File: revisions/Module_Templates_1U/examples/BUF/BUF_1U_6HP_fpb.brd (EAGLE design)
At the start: 28.4 x 28.4 mm, 11 parts, among them J2 ERA-NOSILK

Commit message: Update Backplane Reference
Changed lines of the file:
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@@
 <setting verticaltext="up"/>
 </settings>
-<grid distance="10" unitdist="mil" unit="mil" style="lines" multiple="10" display="yes" altdistance="0.025" altunitdist="inch" altunit="inch"/>
+<grid distance="10" unitdist="mil" unit="mm" style="lines" multiple="10" display="yes" altdistance="0.025" altunitdist="inch" altunit="inch"/>
 <layers>
 <layer number="1" name="Top" color="4" fill="1" visible="no" active="yes"/>
@@
 <layer number="220" name="220bmp" color="21" fill="1" visible="no" active="no"/>
 <layer number="221" name="221bmp" color="22" fill="1" visible="no" active="no"/>
-<layer number="222" name="222bmp" color="23" fill="1" visible="no" active="no"/>
 <layer number="223" name="223bmp" color="24" fill="1" visible="no" active="no"/>
 <layer number="224" name="224bmp" color="25" fill="1" visible="no" active="no"/>
@@
 <circle x="5.08" y="40.1828" radius="1.905" width="0.4064" layer="51"/>
 <circle x="5.08" y="2.9972" radius="1.9235375" width="0.4064" layer="51"/>
-<text x="8.382" y="7.62" size="1.27" layer="21" font="vector" ratio="20">Halcyon Modular</text>
 <text x="23.876" y="8.89" size="1.27" layer="22" font="vector" ratio="20" rot="R180">Halcyon Modular</text>
 </plain>

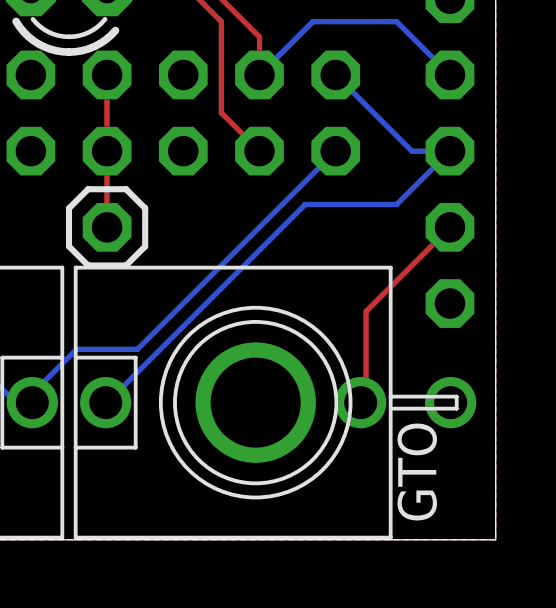
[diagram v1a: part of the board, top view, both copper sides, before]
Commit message: update backplane images
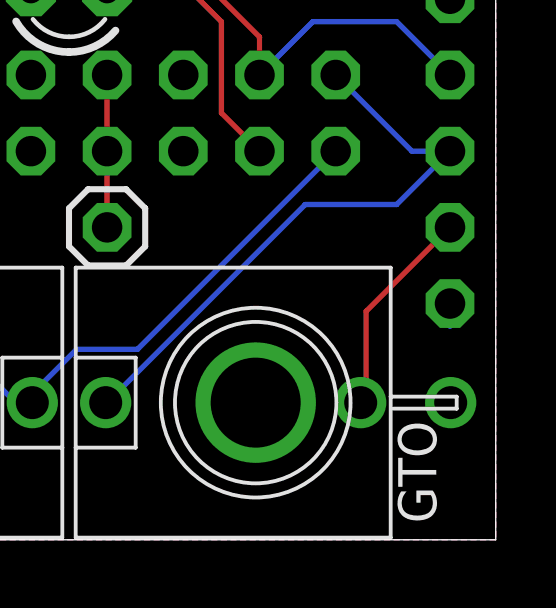
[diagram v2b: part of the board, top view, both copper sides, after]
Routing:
- net GND: track 0.00 -> 0.76 mm
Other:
- board text removed: "Halcyon Modular"
